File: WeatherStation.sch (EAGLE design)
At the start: 17 parts, among them J1 EDISON_CONNECTOR_FULLMOUNTING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, J2 EDISON_CONNECTOR_FULLHEADER, U1 MCP73831

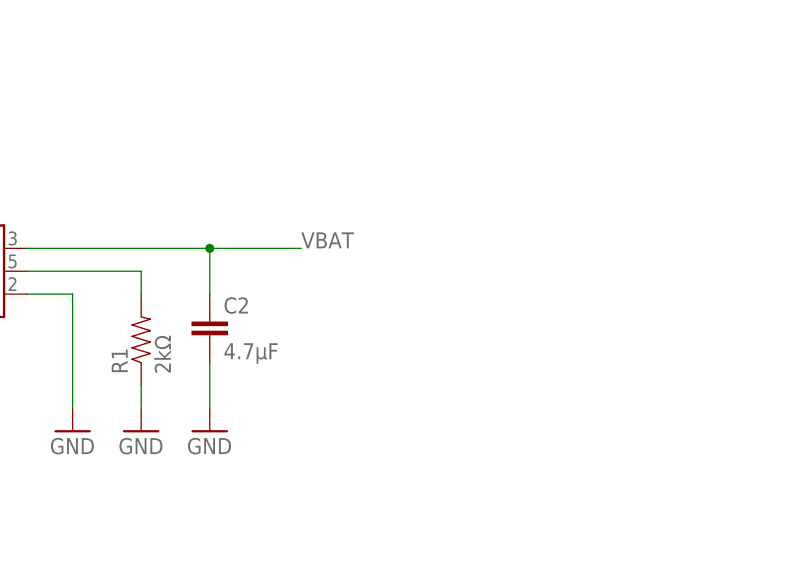
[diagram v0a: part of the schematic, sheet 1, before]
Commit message: added 0.1" 2-pin battery header
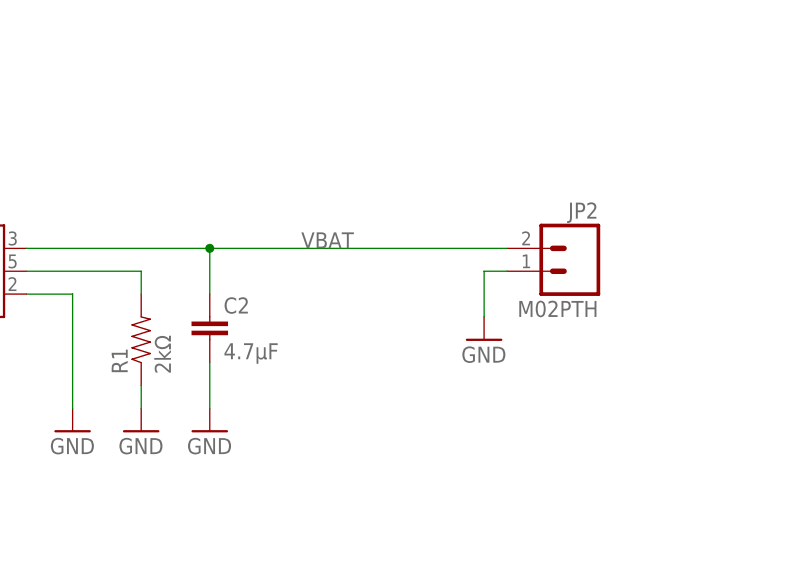
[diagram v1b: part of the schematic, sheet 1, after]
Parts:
- added JP2: M02PTH, SparkFun-Connectors:M02PTH
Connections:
- net GND: now also JP2.1
- net VBAT: now also JP2.2
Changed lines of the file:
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@@
 <part name="LED1" library="SparkFun-LED" deviceset="LED" device="0603"/>
 <part name="R2" library="SparkFun-Resistors" deviceset="RESISTOR" device="0603-RES" value="330Ω"/>
+<part name="JP2" library="SparkFun-Connectors" deviceset="M02" device="PTH"/>
+<part name="GND8" library="SparkFun-Aesthetics" deviceset="GND" device=""/>
 </parts>
 <sheets>
@@
 <instance part="LED1" gate="G$1" x="81.28" y="121.92"/>
 <instance part="R2" gate="G$1" x="91.44" y="114.3" rot="R180"/>
+<instance part="JP2" gate="G$1" x="185.42" y="127" rot="MR0"/>
+<instance part="GND8" gate="1" x="175.26" y="119.38"/>
 </instances>
 <busses>
@@
 <wire x1="129.54" y1="124.46" x2="129.54" y2="111.76" width="0.1524" layer="91"/>
 </segment>
+<segment>
+<pinref part="JP2" gate="G$1" pin="1"/>
+<pinref part="GND8" gate="1" pin="GND"/>
+<wire x1="177.8" y1="127" x2="175.26" y2="127" width="0.1524" layer="91"/>
+<wire x1="175.26" y1="127" x2="175.26" y2="121.92" width="0.1524" layer="91"/>
+</segment>
 </net>
 <net name="VBAT" class="0">
@@
 <wire x1="124.46" y1="129.54" x2="144.78" y2="129.54" width="0.1524" layer="91"/>
 <pinref part="C2" gate="G$1" pin="1"/>
-<wire x1="144.78" y1="129.54" x2="154.94" y2="129.54" width="0.1524" layer="91"/>
 <wire x1="144.78" y1="129.54" x2="144.78" y2="124.46" width="0.1524" layer="91"/>
 <junction x="144.78" y="129.54"/>
 <label x="154.94" y="129.54" size="1.778" layer="95"/>
+<pinref part="JP2" gate="G$1" pin="2"/>
+<wire x1="144.78" y1="129.54" x2="177.8" y2="129.54" width="0.1524" layer="91"/>
 </segment>
 </net>

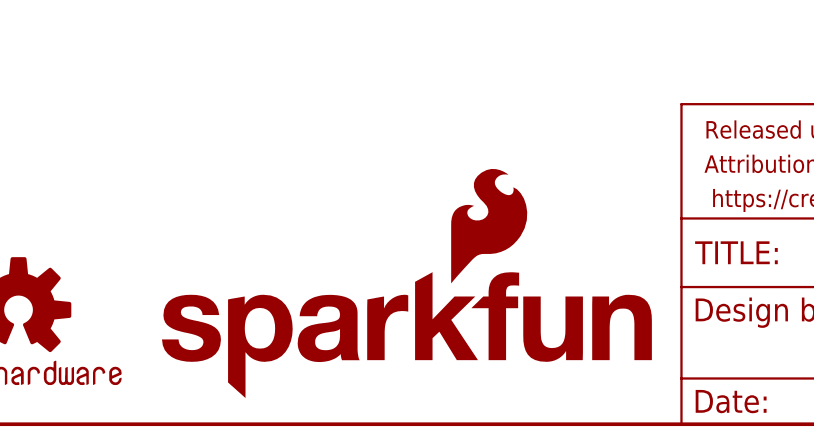
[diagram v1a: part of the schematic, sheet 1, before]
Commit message: moved charge circuit and cleaned up some
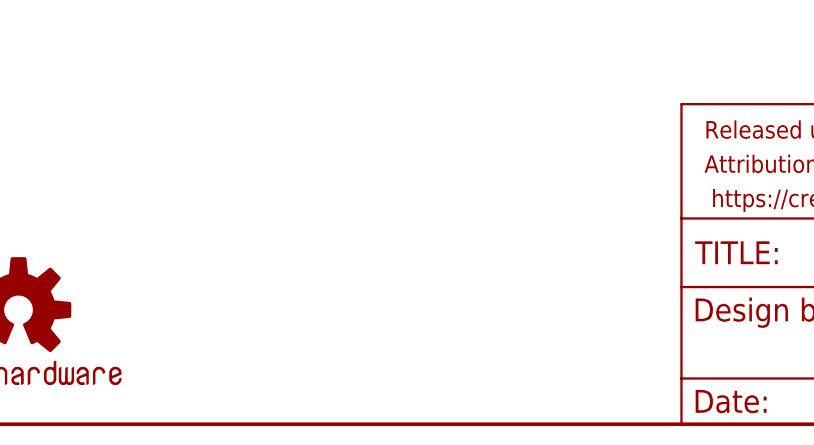
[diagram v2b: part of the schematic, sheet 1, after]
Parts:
- removed LOGO4: SFE_LOGO_NAME_FLAME.1_INCH, SparkFun-Aesthetics:SFE_LOGO_NAME_FLAME.1_INCH
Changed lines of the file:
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@@
 <grid distance="0.1" unitdist="inch" unit="inch" style="lines" multiple="1" display="no" altdistance="0.01" altunitdist="inch" altunit="inch"/>
 <layers>
-<layer number="1" name="Top" color="4" fill="1" visible="yes" active="no"/>
-<layer number="2" name="Route2" color="1" fill="3" visible="yes" active="no"/>
-<layer number="3" name="Route3" color="4" fill="3" visible="yes" active="no"/>
-<layer number="4" name="Route4" color="1" fill="4" visible="yes" active="no"/>
-<layer number="5" name="Route5" color="4" fill="4" visible="yes" active="no"/>
-<layer number="6" name="Route6" color="1" fill="8" visible="yes" active="no"/>
-<layer number="7" name="Route7" color="4" fill="8" visible="yes" active="no"/>
-<layer number="8" name="Route8" color="1" fill="2" visible="yes" active="no"/>
-<layer number="9" name="Route9" color="4" fill="2" visible="yes" active="no"/>
-<layer number="10" name="Route10" color="1" fill="7" visible="yes" active="no"/>
-<layer number="11" name="Route11" color="4" fill="7" visible="yes" active="no"/>
-<layer number="12" name="Route12" color="1" fill="5" visible="yes" active="no"/>
-<layer number="13" name="Route13" color="4" fill="5" visible="yes" active="no"/>
-<layer number="14" name="Route14" color="1" fill="6" visible="yes" active="no"/>
-<layer number="15" name="Route15" color="4" fill="6" visible="yes" active="no"/>
-<layer number="16" name="Bottom" color="1" fill="1" visible="yes" active="no"/>
-<layer number="17" name="Pads" color="2" fill="1" visible="yes" active="no"/>
-<layer number="18" name="Vias" color="2" fill="1" visible="yes" active="no"/>
-<layer number="19" name="Unrouted" color="6" fill="1" visible="yes" active="no"/>
-<layer number="20" name="Dimension" color="15" fill="1" visible="yes" active="no"/>
-<layer number="21" name="tPlace" color="16" fill="1" visible="yes" active="no"/>
-<layer number="22" name="bPlace" color="14" fill="1" visible="yes" active="no"/>
-<layer number="23" name="tOrigins" color="15" fill="1" visible="yes" active="no"/>
-<layer number="24" name="bOrigins" color="15" fill="1" visible="yes" active="no"/>
-<layer number="25" name="tNames" color="7" fill="1" visible="yes" active="no"/>
-<layer number="26" name="bNames" color="7" fill="1" visible="yes" active="no"/>
-<layer number="27" name="tValues" color="7" fill="1" visible="yes" active="no"/>
-<layer number="28" name="bValues" color="7" fill="1" visible="yes" active="no"/>
+<layer number="1" name="Top" color="4" fill="1" visible="no" active="no"/>
+<layer number="2" name="Route2" color="1" fill="3" visible="no" active="no"/>
+<layer number="3" name="Route3" color="4" fill="3" visible="no" active="no"/>
+<layer number="4" name="Route4" color="1" fill="4" visible="no" active="no"/>
+<layer number="5" name="Route5" color="4" fill="4" visible="no" active="no"/>
+<layer number="6" name="Route6" color="1" fill="8" visible="no" active="no"/>
+<layer number="7" name="Route7" color="4" fill="8" visible="no" active="no"/>
+<layer number="8" name="Route8" color="1" fill="2" visible="no" active="no"/>
+<layer number="9" name="Route9" color="4" fill="2" visible="no" active="no"/>
+<layer number="10" name="Route10" color="1" fill="7" visible="no" active="no"/>
+<layer number="11" name="Route11" color="4" fill="7" visible="no" active="no"/>
+<layer number="12" name="Route12" color="1" fill="5" visible="no" active="no"/>
+<layer number="13" name="Route13" color="4" fill="5" visible="no" active="no"/>
+<layer number="14" name="Route14" color="1" fill="6" visible="no" active="no"/>
+<layer number="15" name="Route15" color="4" fill="6" visible="no" active="no"/>
+<layer number="16" name="Bottom" color="1" fill="1" visible="no" active="no"/>
+<layer number="17" name="Pads" color="2" fill="1" visible="no" active="no"/>
+<layer number="18" name="Vias" color="2" fill="1" visible="no" active="no"/>
+<layer number="19" name="Unrouted" color="6" fill="1" visible="no" active="no"/>
+<layer number="20" name="Dimension" color="15" fill="1" visible="no" active="no"/>
+<layer number="21" name="tPlace" color="16" fill="1" visible="no" active="no"/>
+<layer number="22" name="bPlace" color="14" fill="1" visible="no" active="no"/>
+<layer number="23" name="tOrigins" color="15" fill="1" visible="no" active="no"/>
+<layer number="24" name="bOrigins" color="15" fill="1" visible="no" active="no"/>
+<layer number="25" name="tNames" color="7" fill="1" visible="no" active="no"/>
+<layer number="26" name="bNames" color="7" fill="1" visible="no" active="no"/>
+<layer number="27" name="tValues" color="7" fill="1" visible="no" active="no"/>
+<layer number="28" name="bValues" color="7" fill="1" visible="no" active="no"/>
 <layer number="29" name="tStop" color="7" fill="3" visible="no" active="no"/>
 <layer number="30" name="bStop" color="7" fill="6" visible="no" active="no"/>
@@
 <layer number="35" name="tGlue" color="7" fill="4" visible="no" active="no"/>
 <layer number="36" name="bGlue" color="7" fill="5" visible="no" active="no"/>
-<layer number="37" name="tTest" color="7" fill="1" visible="yes" active="no"/>
-<layer number="38" name="bTest" color="7" fill="1" visible="yes" active="no"/>
+<layer number="37" name="tTest" color="7" fill="1" visible="no" active="no"/>
+<layer number="38" name="bTest" color="7" fill="1" visible="no" active="no"/>
 <layer number="39" name="tKeepout" color="4" fill="11" visible="no" active="no"/>
 <layer number="40" name="bKeepout" color="1" fill="11" visible="no" active="no"/>
@@
 <layer number="44" name="Drills" color="7" fill="1" visible="no" active="no"/>
 <layer number="45" name="Holes" color="7" fill="1" visible="no" active="no"/>
-<layer number="46" name="Milling" color="3" fill="1" visible="yes" active="no"/>
-<layer number="47" name="Measures" color="7" fill="1" visible="yes" active="no"/>
-<layer number="48" name="Document" color="7" fill="1" visible="yes" active="no"/>
-<layer number="49" name="Reference" color="7" fill="1" visible="yes" active="no"/>
-<layer number="50" name="dxf" color="7" fill="1" visible="yes" active="no"/>
-<layer number="51" name="tDocu" color="6" fill="1" visible="yes" active="no"/>
-<layer number="52" name="bDocu" color="7" fill="1" visible="yes" active="no"/>
-<layer number="53" name="tGND_GNDA" color="7" fill="9" visible="yes" active="no"/>
-<layer number="54" name="bGND_GNDA" color="1" fill="9" visible="yes" active="no"/>
-<layer number="56" name="wert" color="7" fill="1" visible="yes" active="no"/>
-<layer number="57" name="tCAD" color="7" fill="1" visible="yes" active="no"/>
+<layer number="46" name="Milling" color="3" fill="1" visible="no" active="no"/>
+<layer number="47" name="Measures" color="7" fill="1" visible="no" active="no"/>
+<layer number="48" name="Document" color="7" fill="1" visible="no" active="no"/>
+<layer number="49" name="Reference" color="7" fill="1" visible="no" active="no"/>
+<layer number="50" name="dxf" color="7" fill="1" visible="no" active="no"/>
+<layer number="51" name="tDocu" color="6" fill="1" visible="no" active="no"/>
+<layer number="52" name="bDocu" color="7" fill="1" visible="no" active="no"/>
+<layer number="53" name="tGND_GNDA" color="7" fill="9" visible="no" active="no"/>
+<layer number="54" name="bGND_GNDA" color="1" fill="9" visible="no" active="no"/>
+<layer number="56" name="wert" color="7" fill="1" visible="no" active="no"/>
+<layer number="57" name="tCAD" color="7" fill="1" visible="no" active="no"/>
 <layer number="91" name="Nets" color="2" fill="1" visible="yes" active="yes"/>
 <layer number="92" name="Busses" color="1" fill="1" visible="yes" active="yes"/>
@@
 <part name="FRAME1" library="SparkFun-Aesthetics" deviceset="FRAME-LETTER" device=""/>
 <part name="LOGO1" library="SparkFun-Aesthetics" deviceset="OSHW-LOGO" device="S"/>
-<part name="LOGO4" library="SparkFun-Aesthetics" deviceset="SFE_LOGO_NAME_FLAME" device=".1_INCH"/>
 <part name="J1" library="Edison" deviceset="EDISON_CONNECTOR_FULL" device="MOUNTING_HOLES"/>
 <part name="GND3" library="supply1" deviceset="GND" device=""/>
@@
 <instance part="FRAME1" gate="G$2" x="147.32" y="0"/>
 <instance part="LOGO1" gate="G$1" x="73.66" y="12.7"/>
-<instance part="LOGO4" gate="G$1" x="88.9" y="2.54"/>
 <instance part="FID1" gate="G$1" x="246.38" y="25.4"/>
 <instance part="FID2" gate="G$1" x="241.3" y="25.4"/>
